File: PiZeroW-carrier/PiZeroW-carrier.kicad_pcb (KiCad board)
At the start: 2 copper layers, 65 x 30 mm, 39 parts, among them CON1 BARREL_JACK, J1 PI40HAT, J2 CONN_02X02, P1 USB_OTG, SW1 SW_PUSH, U1 BA50BC0WFP-E2CT, U2 BA06CC0WFP-E2CT, U3 HATconnector

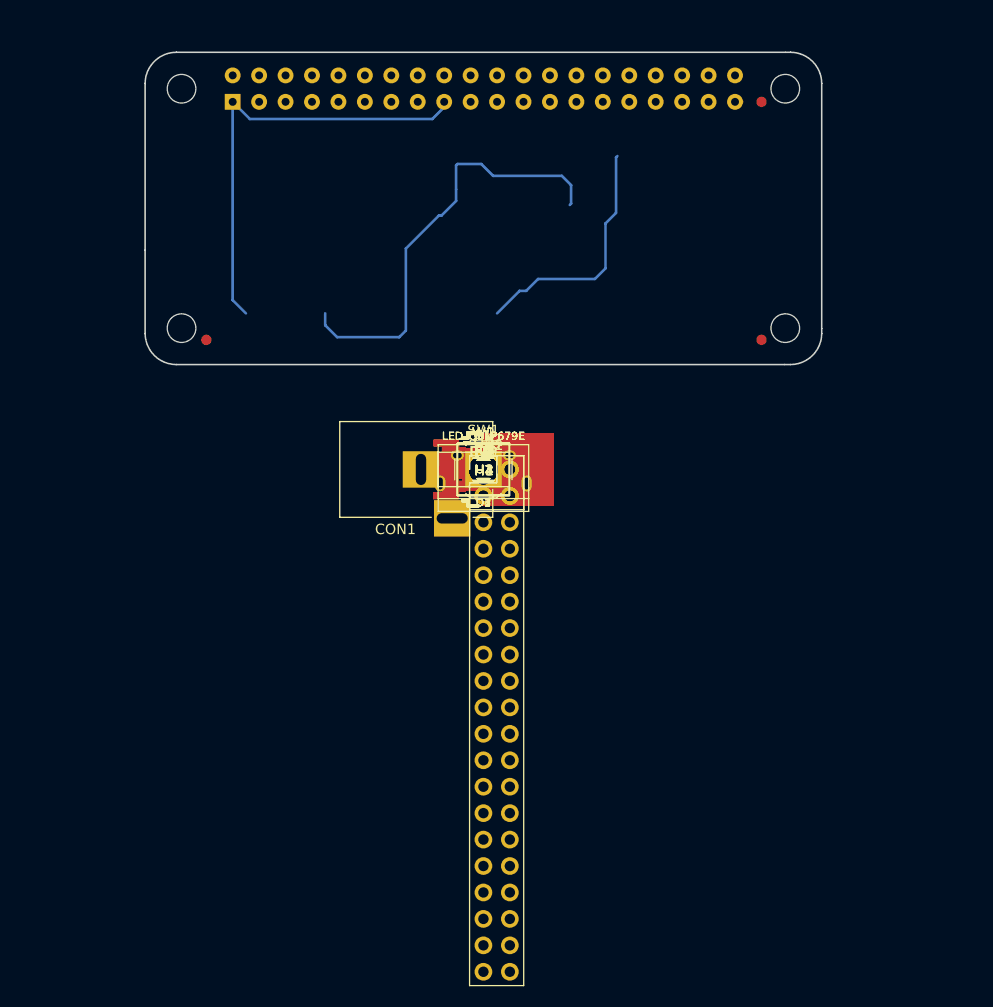
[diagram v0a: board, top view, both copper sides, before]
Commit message: Complete Pizero Layout
Finnished pi zero led PCB board
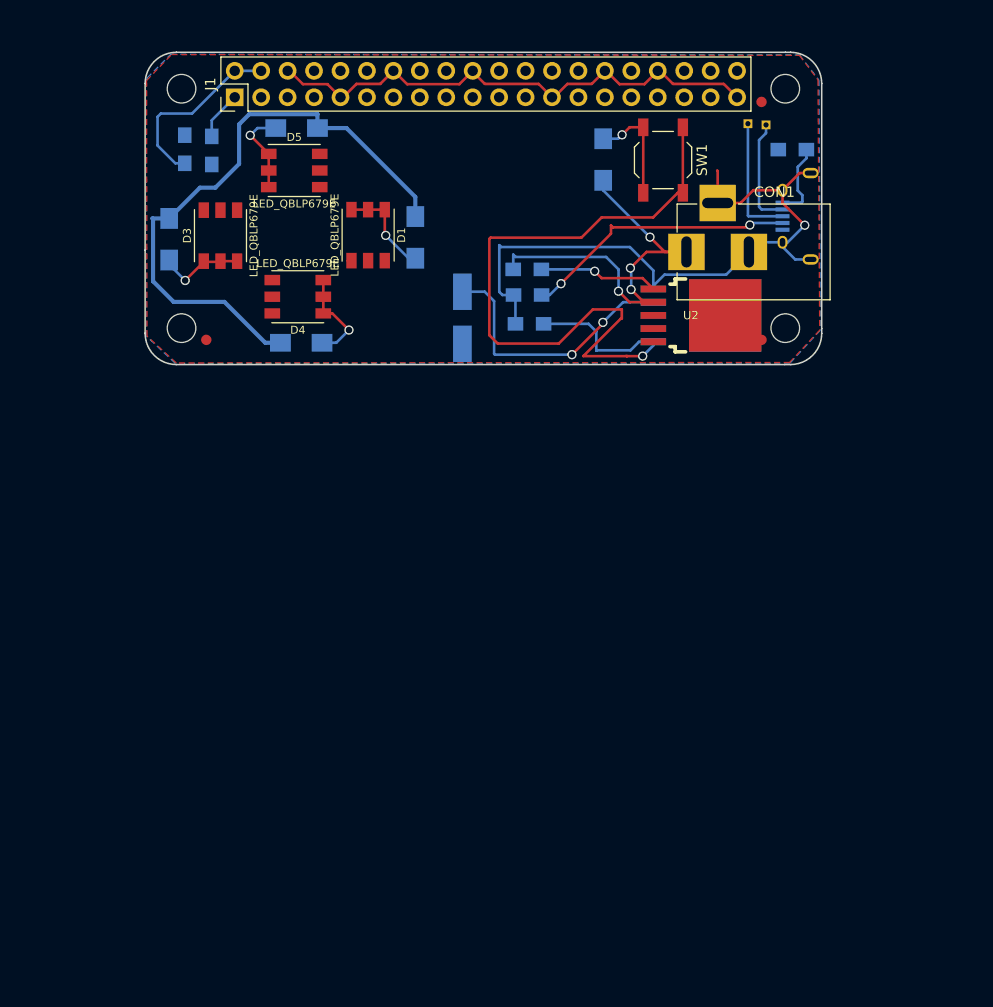
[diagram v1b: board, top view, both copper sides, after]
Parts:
- removed D2: LED_QBLP679E, lib_fp:5050
- removed H1, H2, H3, H4: Hole_3mm_PTH, lib_fp:NPTH_3mm_ID
- removed J2: CONN_02X02, Pin_Headers:Pin_Header_Straight_2x02_Pitch2.54mm
- removed R5: 150, Resistors_SMD:R_1206_HandSoldering
- removed U3: HATconnector, Power:PHAT
- D6, P1, R1, R10, R11, R12, R2, R3, R4, R6, R7, R8, R9, U1: moved to B.Cu
- W1, W2: footprint SMD_Packages:1Pin -> Pin_Headers:Pin_Header_Straight_1x01_Pitch1.00mm; moved to B.Cu
- moved J1 43.0 mm to (118.1, 83.8), turned to 90 degrees
- moved W1 42.8 mm to (169.2, 86.5), turned to 270 degrees
- moved R12 42.7 mm to (171.7, 88.8)
- moved R10 42.1 mm to (113.3, 88.8), turned to 90 degrees
- moved W2 41.8 mm to (167.4, 86.4), turned to 270 degrees
- moved R9 40.3 mm to (115.9, 88.9), turned to 270 degrees
- moved P1 38.7 mm to (172.1, 95.2), turned to 270 degrees
- moved R6 37.4 mm to (111.8, 97.5), turned to 90 degrees
- moved R8 37.4 mm to (124.1, 86.8)
- moved SW1 34.4 mm to (159.3, 89.9), turned to 270 degrees
- moved D5 34.0 mm to (123.8, 90.9), turned to 180 degrees
- moved D3 33.8 mm to (116.7, 97.1), turned to 270 degrees
- moved R1 31.9 mm to (153.5, 89.8), turned to 90 degrees
- moved CON1 28.6 mm to (161.5, 98.7), turned to 180 degrees
- moved D1 25.1 mm to (130.9, 97.1), turned to 90 degrees
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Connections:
- D1 pad 1: /Leds/GND -> GND
- D1 pad 2: /Leds/GND -> GND
- D1 pad 3: /Leds/GND -> GND
- D3 pad 1: /Leds/GND -> GND
- D3 pad 2: /Leds/GND -> GND
- D3 pad 3: /Leds/GND -> GND
- D4 pad 1: /Leds/GND -> GND
- D4 pad 2: /Leds/GND -> GND
- D4 pad 3: /Leds/GND -> GND
- D5 pad 1: /Leds/GND -> GND
- D5 pad 2: /Leds/GND -> GND
- D5 pad 3: /Leds/GND -> GND
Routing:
- net GND: track 1.58 -> 116.9 mm, vias 0 -> 1
- net /Power/PiDisable: track 0.00 -> 77.0 mm, vias 0 -> 1
- net (no net): track 65.0 -> 0.00 mm
- net /Leds/+6V: track 0.00 -> 58.3 mm
- net +3V3: track 43.0 -> 0.00 mm
- net +BATT: track 0.00 -> 40.2 mm, vias 0 -> 4
- net Net-(P1-Pad4): track 0.00 -> 26.6 mm, vias 0 -> 2
- net Net-(D6-Pad2): track 0.00 -> 26.0 mm, vias 0 -> 2
- net /raspberrypi-gpio-40pin/P5V_HAT: track 0.00 -> 18.0 mm
- net Net-(P1-Pad3): track 0.38 -> 12.2 mm
- net /Power/LEDEnable: track 0.00 -> 11.5 mm, vias 0 -> 1
- net Net-(R1-Pad2): track 0.00 -> 10.6 mm, vias 0 -> 1
- net Net-(P1-Pad2): track 0.00 -> 10.5 mm
- net Net-(D1-Pad4): track 0.00 -> 9.46 mm, vias 0 -> 1
- net Net-(D4-Pad4): track 0.00 -> 9.42 mm, vias 0 -> 1
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- added copper zone on B.Cu, net GND
- added copper zone on F.Cu, net GND
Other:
- net class 6v added: clearance 0.254, trace_width 0.4, via_dia 0.889, via_drill 0.635
- net class GND added: clearance 0.254, trace_width 0.254, via_dia 0.889, via_drill 0.635

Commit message: PI Zero PCB finish 2.
2nd finished PCB Attempt before reading new netlist
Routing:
- net GND: track 116.9 -> 30.3 mm, vias 1 -> 0
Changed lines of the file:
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@@
   (general
     (links 65)
-    (no_connects 3)
+    (no_connects 8)
     (area 108.8818 71.35622 178.224 115.09502)
     (thickness 1.6)
     (drawings 12)
-    (tracks 222)
+    (tracks 171)
     (zones 0)
     (modules 31)
@@
     (mod_text_size 1 1)
     (mod_text_width 0.15)
-    (pad_size 1.7 1.7)
-    (pad_drill 1)
+    (pad_size 3.5 3.5)
+    (pad_drill 3)
     (pad_to_mask_clearance 0)
     (aux_axis_origin 117.8687 84.2645)
     (visible_elements 7FFFFFFF)
     (pcbplotparams
-      (layerselection 0x010e8_80000001)
+      (layerselection 0x010fc_80000001)
       (usegerberextensions true)
       (excludeedgelayer true)
@@
       (drillshape 0)
       (scaleselection 1)
-      (outputdirectory ""))
+      (outputdirectory ./))
   )
   (net 0 "")
@@
     (fp_line (start 0.8 4.5) (end 0.8 -4.5) (layer F.Fab) (width 0.1))
     (fp_line (start 0.8 -4.5) (end -13.7 -4.5) (layer F.Fab) (width 0.1))
-    (pad 1 thru_hole rect (at 0 0 180) (size 3.5 3.5) (drill oval 1 3) (layers *.Cu *.Mask)
+    (pad 1 thru_hole rect (at 0 0 180) (size 3.5 3.5) (drill 3) (layers *.Cu *.Mask)
       (net 4 +BATT))
-    (pad 2 thru_hole rect (at -6 0 180) (size 3.5 3.5) (drill oval 1 3) (layers *.Cu *.Mask)
-      (net 1 GND))
-    (pad 3 thru_hole rect (at -3 4.7 180) (size 3.5 3.5) (drill oval 3 1) (layers *.Cu *.Mask)
+    (pad 2 thru_hole rect (at -6 0 180) (size 3.5 3.5) (drill 3) (layers *.Cu *.Mask)
+      (net 1 GND))
+    (pad 3 thru_hole rect (at -3 4.7 180) (size 3.5 3.5) (drill 3) (layers *.Cu *.Mask)
       (net 1 GND))
   )
@@
     (pad 5 smd rect (at 1.3 1.35 180) (size 1.35 0.4) (layers B.Cu B.Paste B.Mask)
       (net 1 GND))
-    (pad 6 thru_hole oval (at -2.5 1.35 180) (size 0.95 1.25) (drill oval 0.55 0.85) (layers *.Cu *.Mask)
-      (net 1 GND))
-    (pad 6 thru_hole oval (at 2.5 1.35 180) (size 0.95 1.25) (drill oval 0.55 0.85) (layers *.Cu *.Mask)
-      (net 1 GND))
-    (pad 6 thru_hole oval (at -4.15 -1.35 180) (size 1.55 1) (drill oval 1.15 0.5) (layers *.Cu *.Mask)
-      (net 1 GND))
-    (pad 6 thru_hole oval (at 4.15 -1.35 180) (size 1.55 1) (drill oval 1.15 0.5) (layers *.Cu *.Mask)
+    (pad 6 thru_hole oval (at -2.5 1.35 180) (size 1.25 1.25) (drill 1) (layers *.Cu *.Mask)
+      (net 1 GND))
+    (pad 6 thru_hole oval (at 2.5 1.35 180) (size 1.25 1.25) (drill 1) (layers *.Cu *.Mask)
+      (net 1 GND))
+    (pad 6 thru_hole oval (at -4.15 -1.35 180) (size 1.25 1.25) (drill oval 1) (layers *.Cu *.Mask)
+      (net 1 GND))
+    (pad 6 thru_hole oval (at 4.15 -1.35 180) (size 1.25 1.25) (drill 1) (layers *.Cu *.Mask)
       (net 1 GND))
   )
@@
   (gr_arc (start 171.5 82.5) (end 171.5 79.5) (angle 90) (layer Edge.Cuts) (width 0.15))
   (gr_arc (start 112.5 82.5) (end 109.5 82.5) (angle 90) (layer Edge.Cuts) (width 0.15))
-  (segment (start 158.75 81.28) (end 158.9532 81.28) (width 0.254) (layer F.Cu) (net 1) (status C00000))
-  (segment (start 158.9532 81.28) (end 160.2105 82.5373) (width 0.254) (layer F.Cu) (net 1) (status 400000))
-  (segment (start 165.0873 82.5373) (end 166.37 83.82) (width 0.254) (layer F.Cu) (net 1) (status 800000))
-  (segment (start 160.2105 82.5373) (end 165.0873 82.5373) (width 0.254) (layer F.Cu) (net 1))
-  (segment (start 153.67 81.28) (end 153.7843 81.28) (width 0.254) (layer F.Cu) (net 1) (status C00000))
-  (segment (start 153.7843 81.28) (end 155.067 82.5627) (width 0.254) (layer F.Cu) (net 1) (status 400000))
-  (segment (start 157.4673 82.5627) (end 158.75 81.28) (width 0.254) (layer F.Cu) (net 1) (status 800000))
-  (segment (start 155.067 82.5627) (end 157.4673 82.5627) (width 0.254) (layer F.Cu) (net 1))
-  (segment (start 148.59 83.82) (end 148.7805 83.82) (width 0.254) (layer F.Cu) (net 1) (status C00000))
-  (segment (start 148.7805 83.82) (end 150.0632 82.5373) (width 0.254) (layer F.Cu) (net 1) (status 400000))
-  (segment (start 152.4127 82.5373) (end 153.67 81.28) (width 0.254) (layer F.Cu) (net 1) (status 800000))
-  (segment (start 150.0632 82.5373) (end 152.4127 82.5373) (width 0.254) (layer F.Cu) (net 1))
-  (segment (start 140.97 81.28) (end 140.97 81.3689) (width 0.254) (layer F.Cu) (net 1) (status C00000))
-  (segment (start 140.97 81.3689) (end 142.1384 82.5373) (width 0.254) (layer F.Cu) (net 1) (status 400000))
-  (segment (start 147.3073 82.5373) (end 148.59 83.82) (width 0.254) (layer F.Cu) (net 1) (status 800000))
-  (segment (start 142.1384 82.5373) (end 147.3073 82.5373) (width 0.254) (layer F.Cu) (net 1))
-  (segment (start 133.35 81.28) (end 133.3881 81.28) (width 0.254) (layer F.Cu) (net 1) (status C00000))
-  (segment (start 133.3881 81.28) (end 134.6708 82.5627) (width 0.254) (layer F.Cu) (net 1) (status 400000))
-  (segment (start 139.6873 82.5627) (end 140.97 81.28) (width 0.254) (layer F.Cu) (net 1) (status 800000))
-  (segment (start 134.6708 82.5627) (end 139.6873 82.5627) (width 0.254) (layer F.Cu) (net 1))
-  (segment (start 128.27 83.82) (end 128.524 83.82) (width 0.254) (layer F.Cu) (net 1) (status C00000))
-  (segment (start 128.524 83.82) (end 129.8067 82.5373) (width 0.254) (layer F.Cu) (net 1) (status 400000))
-  (segment (start 132.0927 82.5373) (end 133.35 81.28) (width 0.254) (layer F.Cu) (net 1) (status 800000))
-  (segment (start 129.8067 82.5373) (end 132.0927 82.5373) (width 0.254) (layer F.Cu) (net 1))
-  (segment (start 123.19 81.28) (end 123.3805 81.28) (width 0.254) (layer F.Cu) (net 1) (status C00000))
-  (segment (start 123.3805 81.28) (end 124.6632 82.5627) (width 0.254) (layer F.Cu) (net 1) (status 400000))
-  (segment (start 124.6632 82.5627) (end 127.0127 82.5627) (width 0.254) (layer F.Cu) (net 1))
-  (segment (start 127.0127 82.5627) (end 128.27 83.82) (width 0.254) (layer F.Cu) (net 1) (status 800000))
   (segment (start 164.5059 93.979) (end 164.5059 90.9094) (width 0.254) (layer F.Cu) (net 1))
   (segment (start 164.5059 90.9094) (end 164.4523 90.8558) (width 0.254) (layer F.Cu) (net 1))
   (segment (start 158.325 102.235) (end 158.325 101.9361) (width 0.254) (layer B.Cu) (net 1))
-  (segment (start 158.325 101.9361) (end 159.3977 100.8634) (width 0.254) (layer B.Cu) (net 1))
-  (segment (start 165.3215 100.8634) (end 167.5059 98.679) (width 0.254) (layer B.Cu) (net 1))
-  (segment (start 159.3977 100.8634) (end 165.3215 100.8634) (width 0.254) (layer B.Cu) (net 1))
   (segment (start 144.8905 102.8192) (end 143.8275 102.8192) (width 0.254) (layer B.Cu) (net 1))
   (segment (start 158.325 100.4638) (end 158.325 102.235) (width 0.254) (layer B.Cu) (net 1))
@@
   (segment (start 145.081 105.5878) (end 145.081 103.0097) (width 0.254) (layer B.Cu) (net 1))
   (segment (start 145.081 103.0097) (end 144.8905 102.8192) (width 0.254) (layer B.Cu) (net 1))
-  (segment (start 170.735 97.75) (end 168.4349 97.75) (width 0.254) (layer B.Cu) (net 1))
-  (segment (start 168.4349 97.75) (end 167.5059 98.679) (width 0.254) (layer B.Cu) (net 1))
-  (segment (start 170.735 97.75) (end 170.735 98.1799) (width 0.254) (layer B.Cu) (net 1))
-  (segment (start 170.735 98.1799) (end 171.9551 99.4) (width 0.254) (layer B.Cu) (net 1))
-  (segment (start 171.9551 99.4) (end 173.435 99.4) (width 0.254) (layer B.Cu) (net 1))
-  (segment (start 170.735 92.75) (end 170.735 93.9762) (width 0.254) (layer F.Cu) (net 1))
-  (segment (start 171.236 97.75) (end 170.735 97.75) (width 0.254) (layer B.Cu) (net 1))
-  (segment (start 172.8724 96.1136) (end 171.236 97.75) (width 0.254) (layer B.Cu) (net 1))
-  (via (at 172.8724 96.1136) (size 0.889) (drill 0.635) (layers F.Cu B.Cu) (net 1))
-  (segment (start 170.735 93.9762) (end 172.8724 96.1136) (width 0.254) (layer F.Cu) (net 1))
-  (segment (start 170.735 92.75) (end 167.9302 92.75) (width 0.254) (layer F.Cu) (net 1))
-  (segment (start 166.7012 93.979) (end 164.5059 93.979) (width 0.254) (layer F.Cu) (net 1))
-  (segment (start 167.9302 92.75) (end 166.7012 93.979) (width 0.254) (layer F.Cu) (net 1))
-  (segment (start 173.435 91.1) (end 172.385 91.1) (width 0.254) (layer F.Cu) (net 1))
-  (segment (start 172.385 91.1) (end 170.735 92.75) (width 0.254) (layer F.Cu) (net 1))
-  (segment (start 166.37 83.82) (end 166.1033 83.82) (width 0.254) (layer F.Cu) (net 1))
-  (segment (start 128.27 83.82) (end 128.5748 83.82) (width 0.254) (layer F.Cu) (net 1))
-  (segment (start 148.39188 84.25942) (end 148.51888 84.25942) (width 0.254) (layer F.Cu) (net 1))
-  (segment (start 166.17188 84.00542) (end 166.17188 84.25942) (width 0.254) (layer F.Cu) (net 1))
-  (segment (start 128.07188 84.25942) (end 128.19888 84.25942) (width 0.254) (layer F.Cu) (net 1))
   (segment (start 129.3243 99.5161) (end 128.9188 99.5161) (width 0.254) (layer F.Cu) (net 1))
   (segment (start 147.5905 102.8192) (end 148.3614 102.8192) (width 0.254) (layer B.Cu) (net 2))

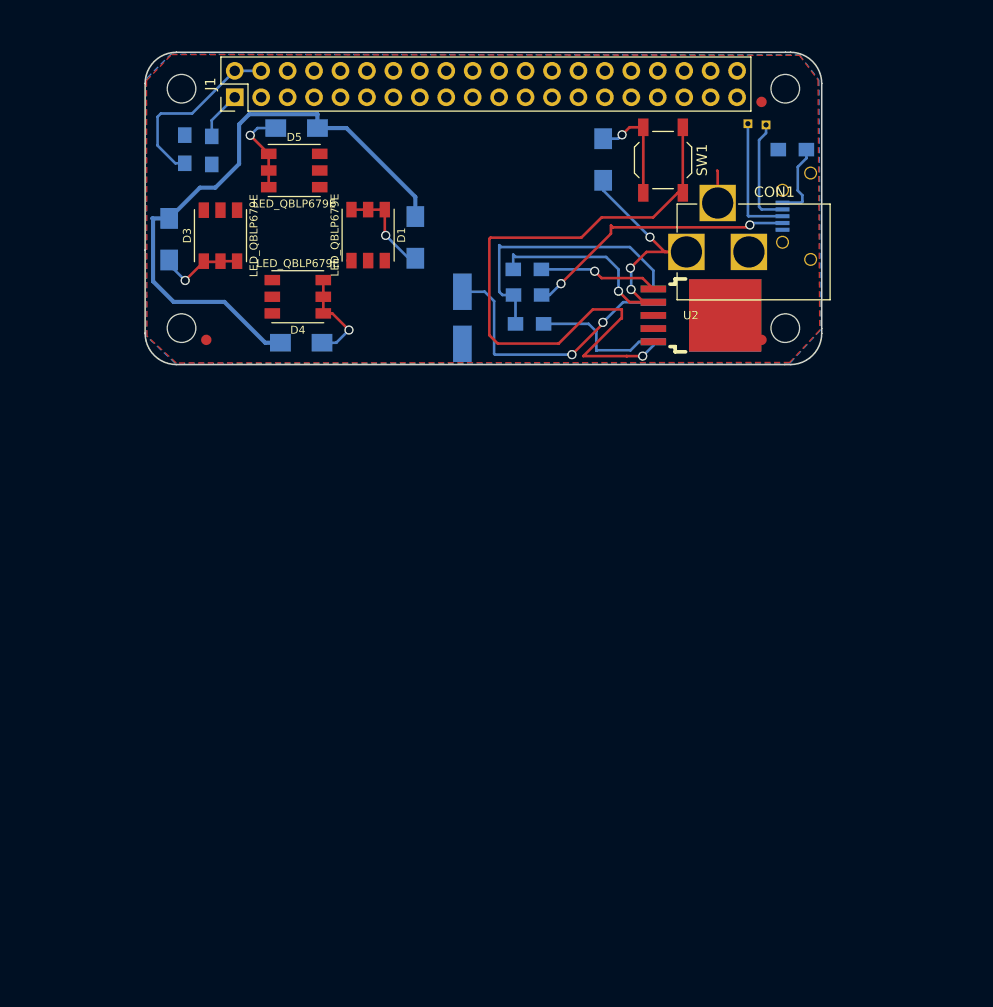
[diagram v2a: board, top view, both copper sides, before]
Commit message: Before Trace fix of LED AND PIDISABLE
Push before tracing fix of LEDEnable and PIDisable
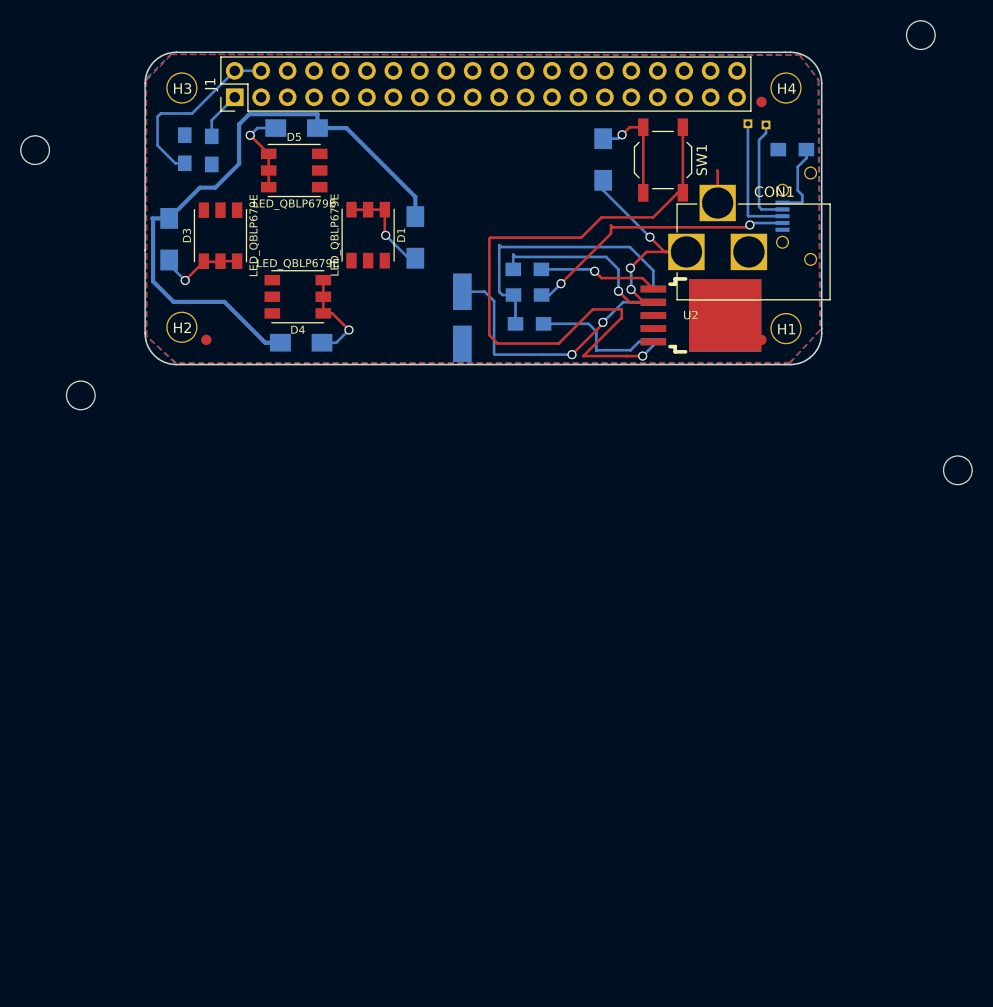
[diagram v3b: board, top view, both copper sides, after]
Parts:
- added H1: Hole_3mm_PTH, lib_fp:NPTH_3mm_ID, F.Cu at (171.1, 106.0)
- added H2: Hole_3mm_PTH, lib_fp:NPTH_3mm_ID, F.Cu at (113.0, 105.9)
- added H3: Hole_3mm_PTH, lib_fp:NPTH_3mm_ID, F.Cu at (113.0, 82.9)
- added H4: Hole_3mm_PTH, lib_fp:NPTH_3mm_ID, F.Cu at (171.1, 82.9)
- moved 1PIN 21.5 mm to (187.6, 119.7)
- moved 1PIN 15.3 mm to (98.9, 88.9)
- moved 1PIN 14.0 mm to (184.0, 77.9)
- moved 1PIN 11.6 mm to (103.3, 112.5)
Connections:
- net /Power/PiDisable renamed Net-(R2-Pad1)
- D1 pad 1: GND -> /Leds/GND
- D1 pad 2: GND -> /Leds/GND
- D1 pad 3: GND -> /Leds/GND
- D3 pad 1: GND -> /Leds/GND
- D3 pad 2: GND -> /Leds/GND
- D3 pad 3: GND -> /Leds/GND
- D4 pad 1: GND -> /Leds/GND
- D4 pad 2: GND -> /Leds/GND
- D4 pad 3: GND -> /Leds/GND
- D5 pad 1: GND -> /Leds/GND
- D5 pad 2: GND -> /Leds/GND
- D5 pad 3: GND -> /Leds/GND
